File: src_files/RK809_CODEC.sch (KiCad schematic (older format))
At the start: 14 parts

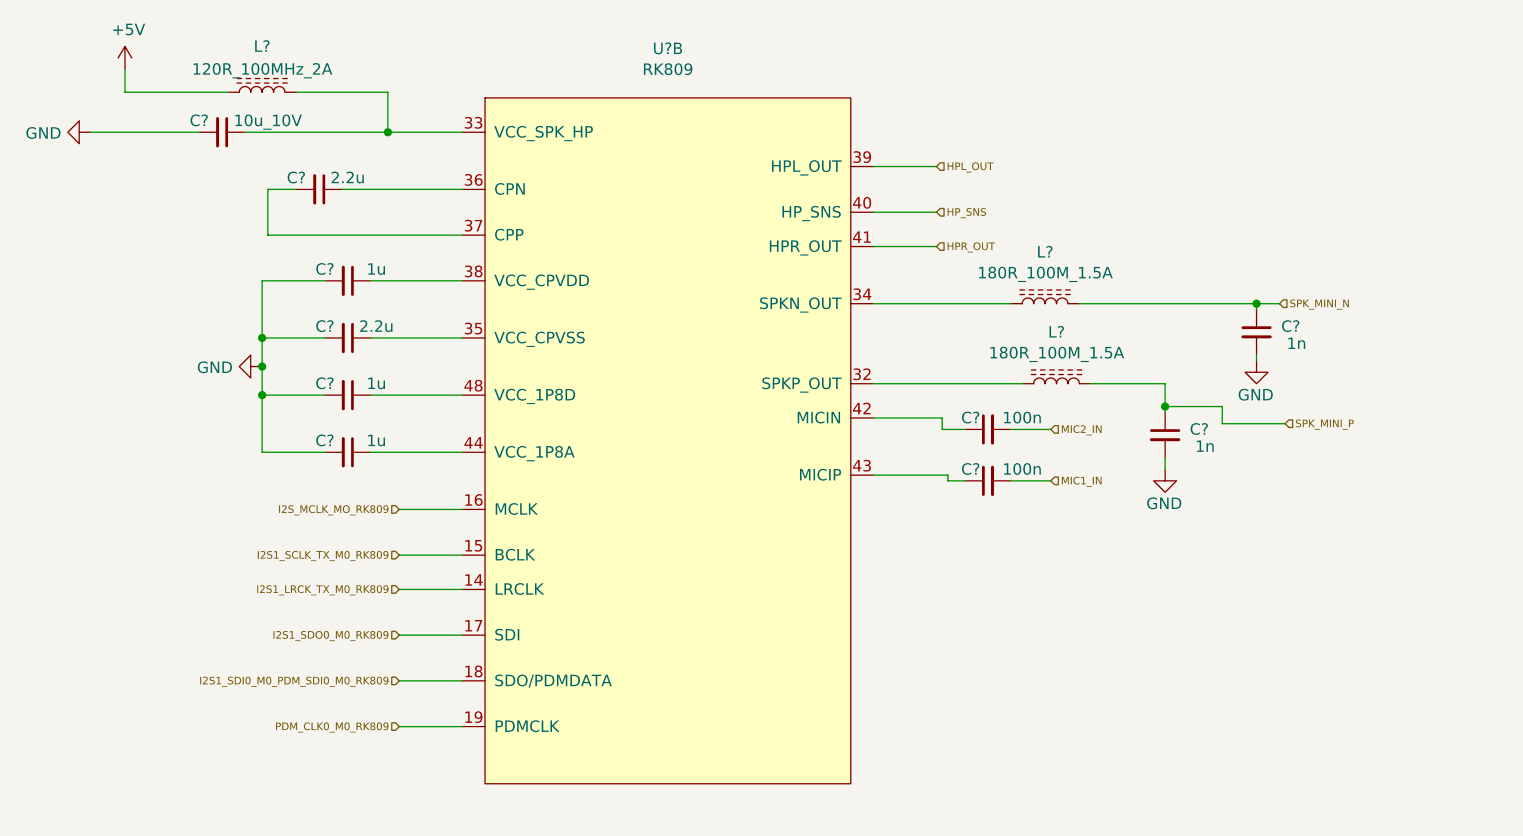
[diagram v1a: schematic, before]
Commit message: LPDDR3 SECTION COMPLETE
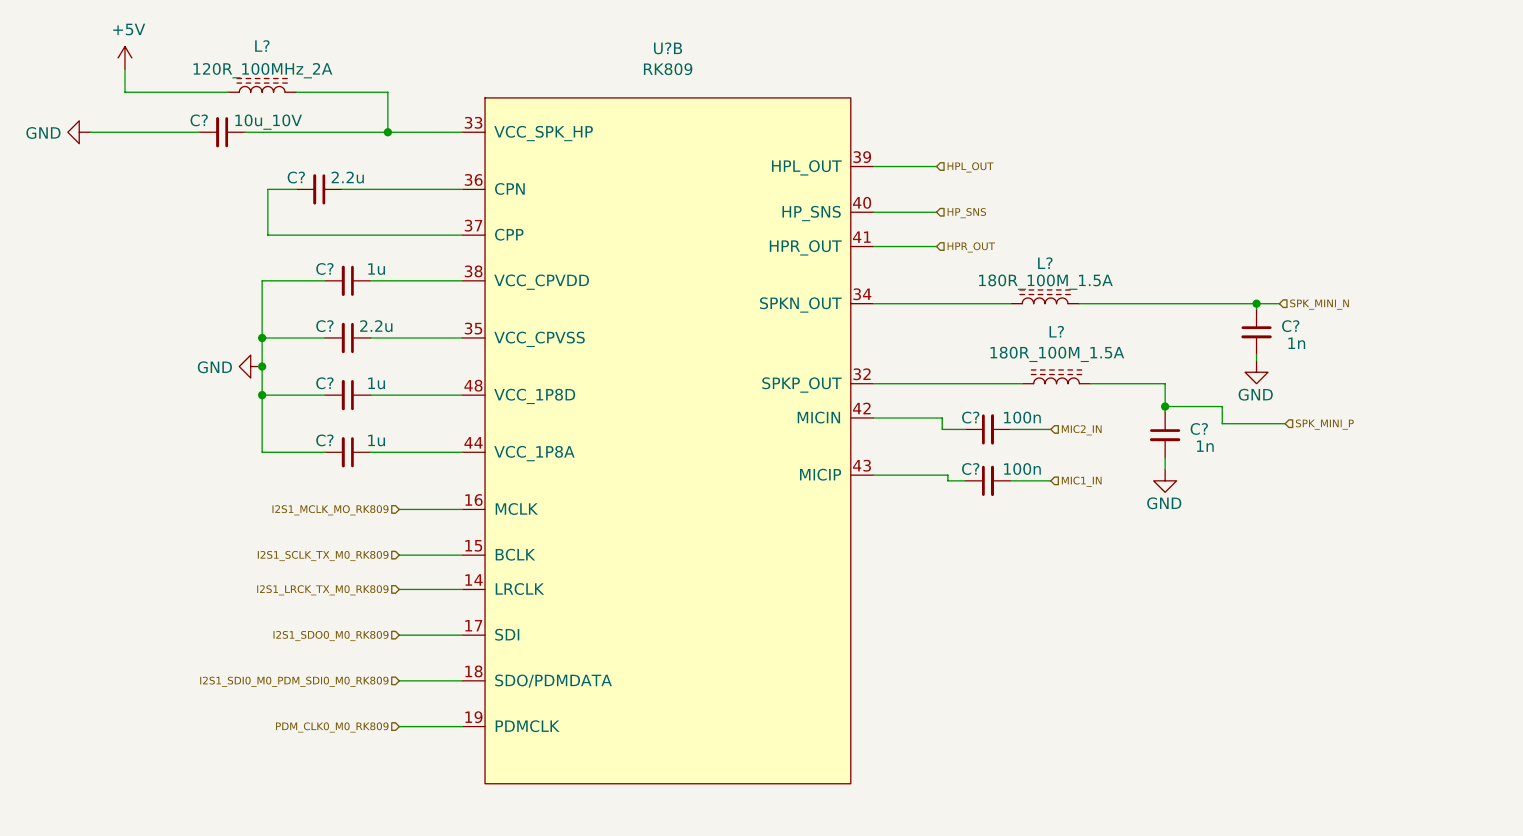
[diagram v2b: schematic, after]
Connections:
- net I2S_MCLK_MO_RK809 renamed I2S1_MCLK_MO_RK809
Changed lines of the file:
@@
 $Descr A4 11693 8268
 encoding utf-8
-Sheet 5 8
+Sheet 7 11
 Title ""
 Date ""
@@
 	3850 2650 4250 2650
 Text HLabel 3975 3650 0    33   Input ~ 0
-I2S_MCLK_MO_RK809
+I2S1_MCLK_MO_RK809
 Wire Wire Line
 	4250 3650 3975 3650
@@
 U 1 1 621EFB2C
 P 6800 2750
-F 0 "L?" V 7025 2750 50  0000 C CNN
-F 1 "180R_100M_1.5A" V 6934 2750 50  0000 C CNN
+F 0 "L?" V 6975 2750 50  0000 C CNN
+F 1 "180R_100M_1.5A" V 6900 2750 50  0000 C CNN
 F 2 "" H 6800 2750 50  0001 C CNN
 F 3 "~" H 6800 2750 50  0001 C CNN

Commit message: littleupdate
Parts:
- C65, C66, C67, C68, C69, C70, C71, C72, C73, C74: renamed from C?; footprint (none) -> Capacitor_SMD:C_0402_1005Metric
- L6, L7, L8: renamed from L?; footprint (none) -> Inductor_SMD:L_0805_2012Metric
- gave numbers to parts that had none: 1
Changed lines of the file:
@@
 $Descr A4 11693 8268
 encoding utf-8
-Sheet 7 11
+Sheet 6 11
 Title ""
 Date ""
@@
 $Comp
 L GCL_Integrated-Circuits:RK809 U?
-U 2 1 621DEE99
+U 3 1 621DEE99
 P 5250 1800
 AR Path="/621DEE99" Ref="U?"  Part="2"
-AR Path="/621DDD46/621DEE99" Ref="U?"  Part="2"
-F 0 "U?" H 5150 1965 50  0000 C CNN
+AR Path="/621DDD46/621DEE99" Ref="U2"  Part="3"
+F 0 "U2" H 5150 1965 50  0000 C CNN
 F 1 "RK809" H 5150 1874 50  0000 C CNN
 F 2 "" H 5150 2000 50  0001 C CNN
 F 3 "" H 5150 2000 50  0001 C CNN
-	2    5250 1800
-	1    0    0    -1
-$EndComp
-$Comp
-L Device:C_Small C?
+	3    5250 1800
+	1    0    0    -1
+$EndComp
+$Comp
+L Device:C_Small C65
 U 1 1 621DF8B5
 P 3200 2000
-F 0 "C?" V 3150 1900 50  0000 C CNN
+F 0 "C65" V 3150 1900 50  0000 C CNN
 F 1 "10u_10V" V 3150 2200 50  0000 C CNN
-F 2 "" H 3200 2000 50  0001 C CNN
+F 2 "Capacitor_SMD:C_0402_1005Metric" H 3200 2000 50  0001 C CNN
 F 3 "~" H 3200 2000 50  0001 C CNN
 	1    3200 2000
@@
 $EndComp
 $Comp
-L OLIMEX_Power:GND #PWR?
+L OLIMEX_Power:GND #PWR0169
 U 1 1 621E189A
 P 2625 2000
-F 0 "#PWR?" H 2625 1750 50  0001 C CNN
+F 0 "#PWR0169" H 2625 1750 50  0001 C CNN
 F 1 "GND" V 2630 1872 50  0000 R CNN
 F 2 "" H 2625 2000 60  0000 C CNN
@@
 	3925 2000 3300 2000
 $Comp
-L power:+5V #PWR?
+L power:+5V #PWR0170
 U 1 1 621E3170
 P 2775 1725
-F 0 "#PWR?" H 2775 1575 50  0001 C CNN
+F 0 "#PWR0170" H 2775 1575 50  0001 C CNN
 F 1 "+5V" H 2790 1898 50  0000 C CNN
 F 2 "" H 2775 1725 50  0001 C CNN
@@
 	2775 1825 3225 1825
 $Comp
-L Device:L_Core_Ferrite L?
+L Device:L_Core_Ferrite L6
 U 1 1 621E3C25
 P 3375 1825
-F 0 "L?" V 3575 1825 50  0000 C CNN
+F 0 "L6" V 3575 1825 50  0000 C CNN
 F 1 "120R_100MHz_2A" V 3475 1825 50  0000 C CNN
-F 2 "" H 3375 1825 50  0001 C CNN
+F 2 "Inductor_SMD:L_0805_2012Metric" H 3375 1825 50  0001 C CNN
 F 3 "~" H 3375 1825 50  0001 C CNN
 	1    3375 1825
@@
 $EndComp
 $Comp
-L Device:C_Small C?
+L Device:C_Small C66
 U 1 1 621E5718
 P 3625 2250
-F 0 "C?" V 3575 2150 50  0000 C CNN
+F 0 "C66" V 3575 2150 50  0000 C CNN
 F 1 "2.2u" V 3575 2375 50  0000 C CNN
-F 2 "" H 3625 2250 50  0001 C CNN
+F 2 "Capacitor_SMD:C_0402_1005Metric" H 3625 2250 50  0001 C CNN
 F 3 "~" H 3625 2250 50  0001 C CNN
 	1    3625 2250
@@
 	3525 2250 3400 2250
 $Comp
-L Device:C_Small C?
+L Device:C_Small C68
 U 1 1 621E6712
 P 3750 2900
-F 0 "C?" V 3700 2800 50  0000 C CNN
+F 0 "C68" V 3700 2800 50  0000 C CNN
 F 1 "2.2u" V 3700 3025 50  0000 C CNN
-F 2 "" H 3750 2900 50  0001 C CNN
+F 2 "Capacitor_SMD:C_0402_1005Metric" H 3750 2900 50  0001 C CNN
 F 3 "~" H 3750 2900 50  0001 C CNN
 	1    3750 2900
@@
 $EndComp
 $Comp
-L Device:C_Small C?
+L Device:C_Small C67
 U 1 1 621E71C3
 P 3750 2650
-F 0 "C?" V 3700 2550 50  0000 C CNN
+F 0 "C67" V 3700 2550 50  0000 C CNN
 F 1 "1u" V 3700 2775 50  0000 C CNN
-F 2 "" H 3750 2650 50  0001 C CNN
+F 2 "Capacitor_SMD:C_0402_1005Metric" H 3750 2650 50  0001 C CNN
 F 3 "~" H 3750 2650 50  0001 C CNN
 	1    3750 2650
@@
 $EndComp
 $Comp
-L Device:C_Small C?
+L Device:C_Small C69
 U 1 1 621E75B0
 P 3750 3150
-F 0 "C?" V 3700 3050 50  0000 C CNN
+F 0 "C69" V 3700 3050 50  0000 C CNN
 F 1 "1u" V 3700 3275 50  0000 C CNN
-F 2 "" H 3750 3150 50  0001 C CNN
+F 2 "Capacitor_SMD:C_0402_1005Metric" H 3750 3150 50  0001 C CNN
 F 3 "~" H 3750 3150 50  0001 C CNN
 	1    3750 3150
@@
 $EndComp
 $Comp
-L Device:C_Small C?
+L Device:C_Small C70
 U 1 1 621E7DC5
 P 3750 3400
-F 0 "C?" V 3700 3300 50  0000 C CNN
+F 0 "C70" V 3700 3300 50  0000 C CNN
 F 1 "1u" V 3700 3525 50  0000 C CNN
-F 2 "" H 3750 3400 50  0001 C CNN
+F 2 "Capacitor_SMD:C_0402_1005Metric" H 3750 3400 50  0001 C CNN
 F 3 "~" H 3750 3400 50  0001 C CNN
 	1    3750 3400
@@
 $EndComp
 $Comp
-L OLIMEX_Power:GND #PWR?
+L OLIMEX_Power:GND #PWR0171
 U 1 1 621E8201
 P 3375 3025
-F 0 "#PWR?" H 3375 2775 50  0001 C CNN
+F 0 "#PWR0171" H 3375 2775 50  0001 C CNN
 F 1 "GND" V 3380 2897 50  0000 R CNN
 F 2 "" H 3375 3025 60  0000 C CNN
@@
 	6325 2500 6050 2500
 $Comp
-L Device:L_Core_Ferrite L?
+L Device:L_Core_Ferrite L7
 U 1 1 621EFB2C
 P 6800 2750
-F 0 "L?" V 6975 2750 50  0000 C CNN
+F 0 "L7" V 6975 2750 50  0000 C CNN
 F 1 "180R_100M_1.5A" V 6900 2750 50  0000 C CNN
-F 2 "" H 6800 2750 50  0001 C CNN
+F 2 "Inductor_SMD:L_0805_2012Metric" H 6800 2750 50  0001 C CNN
 F 3 "~" H 6800 2750 50  0001 C CNN
 	1    6800 2750
@@
 $EndComp
 $Comp
-L Device:L_Core_Ferrite L?
+L Device:L_Core_Ferrite L8
 U 1 1 621F21AF
 P 6850 3100
-F 0 "L?" V 7075 3100 50  0000 C CNN
+F 0 "L8" V 7075 3100 50  0000 C CNN
 F 1 "180R_100M_1.5A" V 6984 3100 50  0000 C CNN
-F 2 "" H 6850 3100 50  0001 C CNN
+F 2 "Inductor_SMD:L_0805_2012Metric" H 6850 3100 50  0001 C CNN
 F 3 "~" H 6850 3100 50  0001 C CNN
 	1    6850 3100
@@
 $EndComp
 $Comp
-L Device:C_Small C?
+L Device:C_Small C73
 U 1 1 621F3391
 P 7325 3325
-F 0 "C?" H 7475 3350 50  0000 C CNN
+F 0 "C73" H 7475 3350 50  0000 C CNN
 F 1 "1n" H 7500 3275 50  0000 C CNN
-F 2 "" H 7325 3325 50  0001 C CNN
+F 2 "Capacitor_SMD:C_0402_1005Metric" H 7325 3325 50  0001 C CNN
 F 3 "~" H 7325 3325 50  0001 C CNN
 	1    7325 3325
@@
 $EndComp
 $Comp
-L Device:C_Small C?
+L Device:C_Small C74
 U 1 1 621F46DF
 P 7725 2875
-F 0 "C?" H 7875 2900 50  0000 C CNN
+F 0 "C74" H 7875 2900 50  0000 C CNN
 F 1 "1n" H 7900 2825 50  0000 C CNN
-F 2 "" H 7725 2875 50  0001 C CNN
+F 2 "Capacitor_SMD:C_0402_1005Metric" H 7725 2875 50  0001 C CNN
 F 3 "~" H 7725 2875 50  0001 C CNN
 	1    7725 2875
@@
 	6650 2750 6050 2750
 $Comp
-L OLIMEX_Power:GND #PWR?
+L OLIMEX_Power:GND #PWR0172
 U 1 1 621F828D
 P 7725 3000
-F 0 "#PWR?" H 7725 2750 50  0001 C CNN
+F 0 "#PWR0172" H 7725 2750 50  0001 C CNN
 F 1 "GND" H 7800 2850 50  0000 R CNN
 F 2 "" H 7725 3000 60  0000 C CNN
@@
 	7725 3000 7725 2975
 $Comp
-L OLIMEX_Power:GND #PWR?
+L OLIMEX_Power:GND #PWR0173
 U 1 1 621FEADE
 P 7325 3475
-F 0 "#PWR?" H 7325 3225 50  0001 C CNN
+F 0 "#PWR0173" H 7325 3225 50  0001 C CNN
 F 1 "GND" H 7400 3325 50  0000 R CNN
 F 2 "" H 7325 3475 60  0000 C CNN
@@
 	7325 3200 7325 3225
 $Comp
-L Device:C_Small C?
+L Device:C_Small C71
 U 1 1 62204B09
 P 6550 3300
-F 0 "C?" V 6600 3375 50  0000 C CNN
+F 0 "C71" V 6600 3375 50  0000 C CNN
 F 1 "100n" V 6600 3150 50  0000 C CNN
-F 2 "" H 6550 3300 50  0001 C CNN
+F 2 "Capacitor_SMD:C_0402_1005Metric" H 6550 3300 50  0001 C CNN
 F 3 "~" H 6550 3300 50  0001 C CNN
 	1    6550 3300
@@
 $EndComp
 $Comp
-L Device:C_Small C?
+L Device:C_Small C72
 U 1 1 622058C7
 P 6550 3525
-F 0 "C?" V 6600 3600 50  0000 C CNN
+F 0 "C72" V 6600 3600 50  0000 C CNN
 F 1 "100n" V 6600 3375 50  0000 C CNN
-F 2 "" H 6550 3525 50  0001 C CNN
+F 2 "Capacitor_SMD:C_0402_1005Metric" H 6550 3525 50  0001 C CNN
 F 3 "~" H 6550 3525 50  0001 C CNN
 	1    6550 3525

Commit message: all screens added_3 items left
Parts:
- removed U2: RK809, symbol GCL_Integrated-Circuits:RK809
- added U2: RK809, symbol GCL_Integrated-Circuits:RK809
